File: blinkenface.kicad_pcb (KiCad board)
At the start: 2 copper layers, 135 x 50 mm, 245 parts, among them J1 CONN_01X04

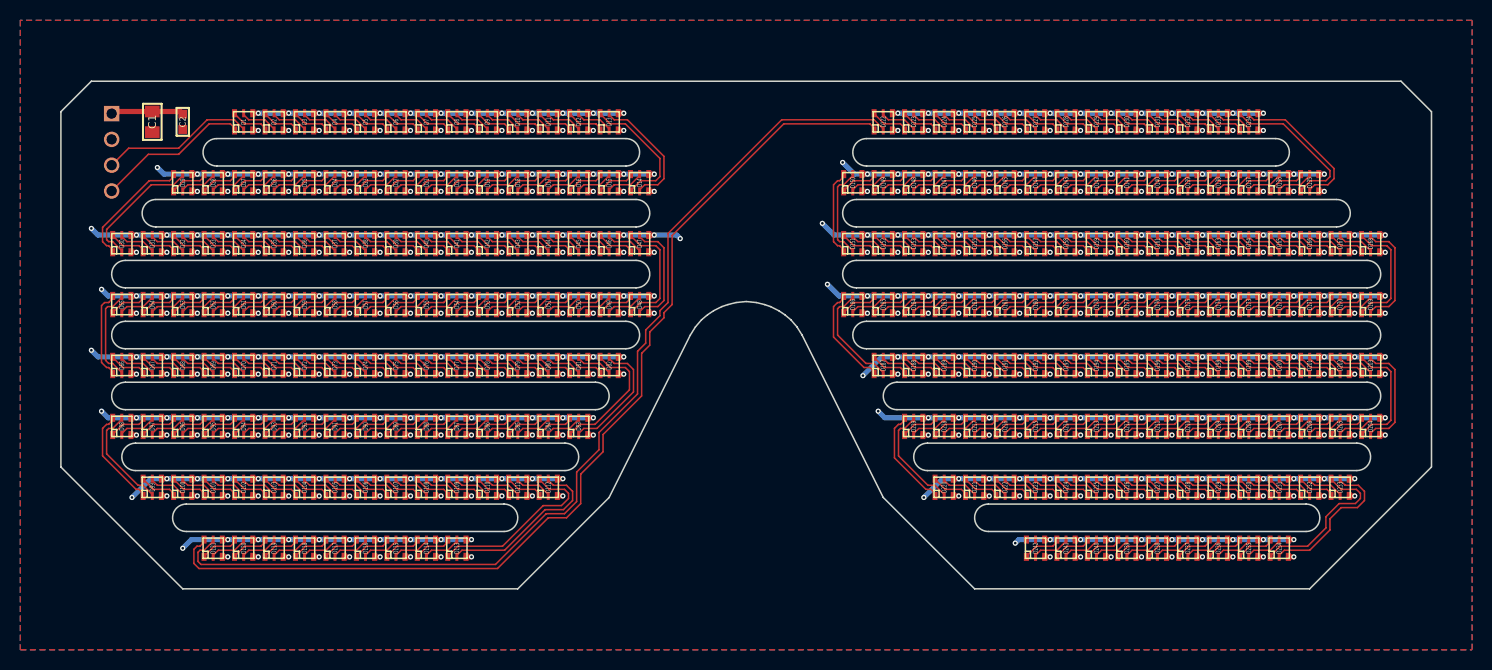
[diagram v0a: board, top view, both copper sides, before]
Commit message: fixed APA102-2020 pin order
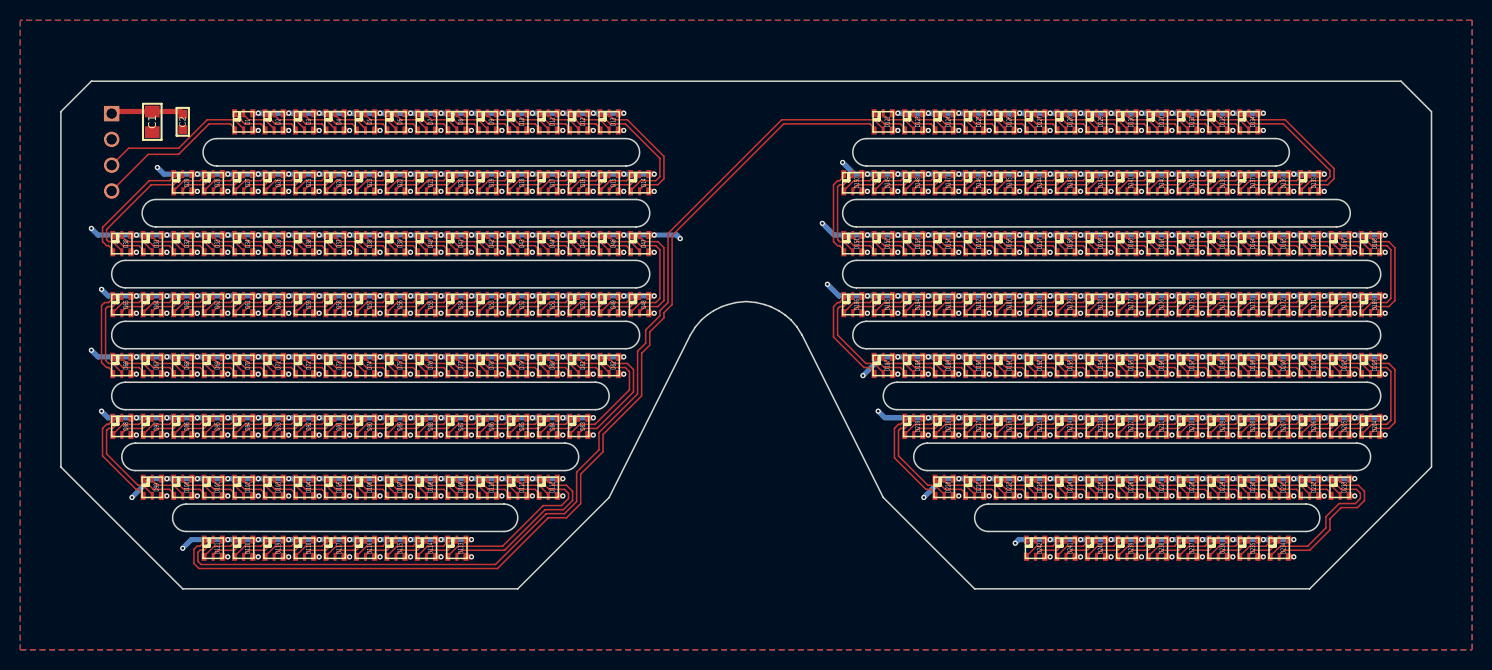
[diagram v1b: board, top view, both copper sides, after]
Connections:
- D1 pad 3: GND -> Net-(D1-Pad3)
- D1 pad 4: VCC -> GND
- D1 pad 5: Net-(D1-Pad5) -> VCC
- D10 pad 3: GND -> Net-(D10-Pad3)
- D10 pad 4: VCC -> GND
- D10 pad 5: Net-(D10-Pad5) -> VCC
- D100 pad 3: GND -> Net-(D100-Pad3)
- D100 pad 4: VCC -> GND
- D100 pad 5: Net-(D100-Pad5) -> VCC
- D101 pad 1: Net-(D100-Pad6) -> Net-(D101-Pad1)
- D101 pad 2: Net-(D100-Pad5) -> Net-(D100-Pad1)
- D101 pad 3: GND -> Net-(D100-Pad6)
- D101 pad 4: VCC -> GND
- D101 pad 5: Net-(D101-Pad5) -> VCC
- D102 pad 1: Net-(D101-Pad6) -> Net-(D102-Pad1)
- D102 pad 2: Net-(D101-Pad5) -> Net-(D101-Pad1)
- D102 pad 3: GND -> Net-(D101-Pad6)
- D102 pad 4: VCC -> GND
- D102 pad 5: Net-(D102-Pad5) -> VCC
- D103 pad 1: Net-(D102-Pad6) -> Net-(D103-Pad1)
- D103 pad 2: Net-(D102-Pad5) -> Net-(D102-Pad1)
- D103 pad 3: GND -> Net-(D102-Pad6)
- D103 pad 4: VCC -> GND
- D103 pad 5: Net-(D103-Pad5) -> VCC
- D104 pad 1: Net-(D103-Pad6) -> Net-(D104-Pad1)
- D104 pad 2: Net-(D103-Pad5) -> Net-(D103-Pad1)
- D104 pad 3: GND -> Net-(D103-Pad6)
- D104 pad 4: VCC -> GND
- D104 pad 5: Net-(D104-Pad5) -> VCC
- D105 pad 1: Net-(D104-Pad6) -> Net-(D105-Pad1)
- D105 pad 2: Net-(D104-Pad5) -> Net-(D104-Pad1)
- D105 pad 3: GND -> Net-(D104-Pad6)
- D105 pad 4: VCC -> GND
- D105 pad 5: Net-(D105-Pad5) -> VCC
- D106 pad 1: Net-(D105-Pad6) -> Net-(D106-Pad1)
- D106 pad 2: Net-(D105-Pad5) -> Net-(D105-Pad1)
- D106 pad 3: GND -> Net-(D105-Pad6)
- D106 pad 4: VCC -> GND
- D106 pad 5: Net-(D106-Pad5) -> VCC
- D107 pad 1: Net-(D106-Pad6) -> Net-(D107-Pad1)
- D107 pad 2: Net-(D106-Pad5) -> Net-(D106-Pad1)
- D107 pad 3: GND -> Net-(D106-Pad6)
- D107 pad 4: VCC -> GND
- D107 pad 5: Net-(D107-Pad5) -> VCC
- D108 pad 1: Net-(D107-Pad6) -> Net-(D108-Pad1)
- D108 pad 2: Net-(D107-Pad5) -> Net-(D107-Pad1)
- D108 pad 3: GND -> Net-(D107-Pad6)
- D108 pad 4: VCC -> GND
- D108 pad 5: Net-(D108-Pad5) -> VCC
- D109 pad 1: Net-(D108-Pad6) -> Net-(D109-Pad1)
- D109 pad 2: Net-(D108-Pad5) -> Net-(D108-Pad1)
- D109 pad 3: GND -> Net-(D108-Pad6)
- D109 pad 4: VCC -> GND
- D109 pad 5: Net-(D109-Pad5) -> VCC
- D11 pad 1: Net-(D10-Pad6) -> Net-(D11-Pad1)
- D11 pad 2: Net-(D10-Pad5) -> Net-(D10-Pad1)
- D11 pad 3: GND -> Net-(D10-Pad6)
- D11 pad 4: VCC -> GND
- D11 pad 5: Net-(D11-Pad5) -> VCC
- D110 pad 1: Net-(D109-Pad6) -> Net-(D110-Pad1)
- D110 pad 2: Net-(D109-Pad5) -> Net-(D109-Pad1)
- D110 pad 3: GND -> Net-(D109-Pad6)
- D110 pad 4: VCC -> GND
- D110 pad 5: Net-(D110-Pad5) -> VCC
- D111 pad 1: Net-(D110-Pad6) -> Net-(D111-Pad1)
- D111 pad 2: Net-(D110-Pad5) -> Net-(D110-Pad1)
- D111 pad 3: GND -> Net-(D110-Pad6)
- D111 pad 4: VCC -> GND
- D111 pad 5: Net-(D111-Pad5) -> VCC
- D112 pad 1: Net-(D111-Pad6) -> Net-(D112-Pad1)
- D112 pad 2: Net-(D111-Pad5) -> Net-(D111-Pad1)
- D112 pad 3: GND -> Net-(D111-Pad6)
- D112 pad 4: VCC -> GND
- D112 pad 5: Net-(D112-Pad5) -> VCC
- D113 pad 1: Net-(D112-Pad6) -> Net-(D113-Pad1)
- D113 pad 2: Net-(D112-Pad5) -> Net-(D112-Pad1)
- D113 pad 3: GND -> Net-(D112-Pad6)
- D113 pad 4: VCC -> GND
- D113 pad 5: Net-(D113-Pad5) -> VCC
- D114 pad 1: Net-(D113-Pad6) -> Net-(D114-Pad1)
- D114 pad 2: Net-(D113-Pad5) -> Net-(D113-Pad1)
- D114 pad 3: GND -> Net-(D113-Pad6)
- D114 pad 4: VCC -> GND
- D114 pad 5: Net-(D114-Pad5) -> VCC
- D115 pad 1: Net-(D114-Pad6) -> Net-(D115-Pad1)
- D115 pad 2: Net-(D114-Pad5) -> Net-(D114-Pad1)
- D115 pad 3: GND -> Net-(D114-Pad6)
- D115 pad 4: VCC -> GND
- D115 pad 5: Net-(D115-Pad5) -> VCC
- D116 pad 1: Net-(D115-Pad6) -> Net-(D116-Pad1)
- D116 pad 2: Net-(D115-Pad5) -> Net-(D115-Pad1)
- D116 pad 3: GND -> Net-(D115-Pad6)
- D116 pad 4: VCC -> GND
- D116 pad 5: Net-(D116-Pad5) -> VCC
- D117 pad 1: Net-(D116-Pad6) -> Net-(D117-Pad1)
- D117 pad 2: Net-(D116-Pad5) -> Net-(D116-Pad1)
- D117 pad 3: GND -> Net-(D116-Pad6)
- D117 pad 4: VCC -> GND
- D117 pad 5: Net-(D117-Pad5) -> VCC
- D118 pad 1: Net-(D117-Pad6) -> Net-(D118-Pad1)
- D118 pad 2: Net-(D117-Pad5) -> Net-(D117-Pad1)
- D118 pad 3: GND -> Net-(D117-Pad6)
- D118 pad 4: VCC -> GND
- D118 pad 5: Net-(D118-Pad5) -> VCC
- D119 pad 1: Net-(D118-Pad6) -> Net-(D119-Pad1)
- D119 pad 2: Net-(D118-Pad5) -> Net-(D118-Pad1)
- D119 pad 3: GND -> Net-(D118-Pad6)
- D119 pad 4: VCC -> GND
- D119 pad 5: Net-(D119-Pad5) -> VCC
- D12 pad 1: Net-(D11-Pad6) -> Net-(D12-Pad1)
- D12 pad 2: Net-(D11-Pad5) -> Net-(D11-Pad1)
- D12 pad 3: GND -> Net-(D11-Pad6)
- D12 pad 4: VCC -> GND
- D12 pad 5: Net-(D12-Pad5) -> VCC
- D120 pad 1: Net-(D119-Pad6) -> Net-(D120-Pad1)
- D120 pad 2: Net-(D119-Pad5) -> Net-(D119-Pad1)
- D120 pad 3: GND -> Net-(D119-Pad6)
- D120 pad 4: VCC -> GND
- D120 pad 5: Net-(D120-Pad5) -> VCC
- D121 pad 1: Net-(D120-Pad6) -> Net-(D121-Pad1)
- D121 pad 2: Net-(D120-Pad5) -> Net-(D120-Pad1)
- D121 pad 3: GND -> Net-(D120-Pad6)
- D121 pad 4: VCC -> GND
- D121 pad 5: Net-(D121-Pad5) -> VCC
- D122 pad 1: Net-(D121-Pad6) -> Net-(D122-Pad1)
- D122 pad 2: Net-(D121-Pad5) -> Net-(D121-Pad1)
- D122 pad 3: GND -> Net-(D121-Pad6)
- D122 pad 4: VCC -> GND
- D122 pad 5: Net-(D122-Pad5) -> VCC
- D123 pad 1: Net-(D122-Pad6) -> Net-(D123-Pad1)
- D123 pad 2: Net-(D122-Pad5) -> Net-(D122-Pad1)
- D123 pad 3: GND -> Net-(D122-Pad6)
- D123 pad 4: VCC -> GND
- D123 pad 5: Net-(D123-Pad5) -> VCC
- D124 pad 1: Net-(D123-Pad6) -> Net-(D124-Pad1)
- D124 pad 2: Net-(D123-Pad5) -> Net-(D123-Pad1)
- D124 pad 3: GND -> Net-(D123-Pad6)
- D124 pad 4: VCC -> GND
- D124 pad 5: Net-(D124-Pad5) -> VCC
- D125 pad 1: Net-(D124-Pad6) -> Net-(D125-Pad1)
- D125 pad 2: Net-(D124-Pad5) -> Net-(D124-Pad1)
- D125 pad 3: GND -> Net-(D124-Pad6)
- D125 pad 4: VCC -> GND
- D125 pad 5: Net-(D125-Pad5) -> VCC
- D126 pad 1: Net-(D125-Pad6) -> Net-(D126-Pad1)
- D126 pad 2: Net-(D125-Pad5) -> Net-(D125-Pad1)
- D126 pad 3: GND -> Net-(D125-Pad6)
- D126 pad 4: VCC -> GND
- D126 pad 5: Net-(D126-Pad5) -> VCC
- D127 pad 1: Net-(D126-Pad6) -> Net-(D127-Pad1)
- D127 pad 2: Net-(D126-Pad5) -> Net-(D126-Pad1)
- D127 pad 3: GND -> Net-(D126-Pad6)
- D127 pad 4: VCC -> GND
- D127 pad 5: Net-(D127-Pad5) -> VCC
- D128 pad 1: Net-(D127-Pad6) -> Net-(D128-Pad1)
- D128 pad 2: Net-(D127-Pad5) -> Net-(D127-Pad1)
- D128 pad 3: GND -> Net-(D127-Pad6)
- D128 pad 4: VCC -> GND
- D128 pad 5: Net-(D128-Pad5) -> VCC
- D129 pad 1: Net-(D128-Pad6) -> Net-(D129-Pad1)
- D129 pad 2: Net-(D128-Pad5) -> Net-(D128-Pad1)
- D129 pad 3: GND -> Net-(D128-Pad6)
- D129 pad 4: VCC -> GND
- D129 pad 5: Net-(D129-Pad5) -> VCC
- D13 pad 1: Net-(D12-Pad6) -> Net-(D13-Pad1)
- D13 pad 2: Net-(D12-Pad5) -> Net-(D12-Pad1)
- D13 pad 3: GND -> Net-(D12-Pad6)
- D13 pad 4: VCC -> GND
- D13 pad 5: Net-(D13-Pad5) -> VCC
- D130 pad 1: Net-(D129-Pad6) -> Net-(D130-Pad1)
- D130 pad 2: Net-(D129-Pad5) -> Net-(D129-Pad1)
- D130 pad 3: GND -> Net-(D129-Pad6)
- D130 pad 4: VCC -> GND
- D130 pad 5: Net-(D130-Pad5) -> VCC
- D131 pad 1: Net-(D130-Pad6) -> Net-(D131-Pad1)
- D131 pad 2: Net-(D130-Pad5) -> Net-(D130-Pad1)
- D131 pad 3: GND -> Net-(D130-Pad6)
- D131 pad 4: VCC -> GND
- D131 pad 5: Net-(D131-Pad5) -> VCC
- D132 pad 1: Net-(D131-Pad6) -> Net-(D132-Pad1)
- D132 pad 2: Net-(D131-Pad5) -> Net-(D131-Pad1)
- D132 pad 3: GND -> Net-(D131-Pad6)
- D132 pad 4: VCC -> GND
- D132 pad 5: Net-(D132-Pad5) -> VCC
- D133 pad 1: Net-(D132-Pad6) -> Net-(D133-Pad1)
- D133 pad 2: Net-(D132-Pad5) -> Net-(D132-Pad1)
- D133 pad 3: GND -> Net-(D132-Pad6)
- D133 pad 4: VCC -> GND
- D133 pad 5: Net-(D133-Pad5) -> VCC
- D134 pad 1: Net-(D133-Pad6) -> Net-(D134-Pad1)
- D134 pad 2: Net-(D133-Pad5) -> Net-(D133-Pad1)
- D134 pad 3: GND -> Net-(D133-Pad6)
- D134 pad 4: VCC -> GND
- D134 pad 5: Net-(D134-Pad5) -> VCC
- D135 pad 1: Net-(D134-Pad6) -> Net-(D135-Pad1)
- D135 pad 2: Net-(D134-Pad5) -> Net-(D134-Pad1)
- D135 pad 3: GND -> Net-(D134-Pad6)
- D135 pad 4: VCC -> GND
- D135 pad 5: Net-(D135-Pad5) -> VCC
- D136 pad 1: Net-(D135-Pad6) -> Net-(D136-Pad1)
- D136 pad 2: Net-(D135-Pad5) -> Net-(D135-Pad1)
- D136 pad 3: GND -> Net-(D135-Pad6)
- D136 pad 4: VCC -> GND
- D136 pad 5: Net-(D136-Pad5) -> VCC
- D137 pad 1: Net-(D136-Pad6) -> Net-(D137-Pad1)
- D137 pad 2: Net-(D136-Pad5) -> Net-(D136-Pad1)
- D137 pad 3: GND -> Net-(D136-Pad6)
- D137 pad 4: VCC -> GND
- D137 pad 5: Net-(D137-Pad5) -> VCC
- D138 pad 1: Net-(D137-Pad6) -> Net-(D138-Pad1)
- D138 pad 2: Net-(D137-Pad5) -> Net-(D137-Pad1)
- D138 pad 3: GND -> Net-(D137-Pad6)
- D138 pad 4: VCC -> GND
- D138 pad 5: Net-(D138-Pad5) -> VCC
- D139 pad 1: Net-(D138-Pad6) -> Net-(D139-Pad1)
- D139 pad 2: Net-(D138-Pad5) -> Net-(D138-Pad1)
- D139 pad 3: GND -> Net-(D138-Pad6)
- D139 pad 4: VCC -> GND
- D139 pad 5: Net-(D139-Pad5) -> VCC
- D14 pad 1: Net-(D13-Pad6) -> Net-(D14-Pad1)
- D14 pad 2: Net-(D13-Pad5) -> Net-(D13-Pad1)
- D14 pad 3: GND -> Net-(D13-Pad6)
- D14 pad 4: VCC -> GND
- D14 pad 5: Net-(D14-Pad5) -> VCC
- D140 pad 1: Net-(D139-Pad6) -> Net-(D140-Pad1)
- D140 pad 2: Net-(D139-Pad5) -> Net-(D139-Pad1)
- D140 pad 3: GND -> Net-(D139-Pad6)
- D140 pad 4: VCC -> GND
- D140 pad 5: Net-(D140-Pad5) -> VCC
- D141 pad 1: Net-(D140-Pad6) -> Net-(D141-Pad1)
- D141 pad 2: Net-(D140-Pad5) -> Net-(D140-Pad1)
- D141 pad 3: GND -> Net-(D140-Pad6)
- D141 pad 4: VCC -> GND
- D141 pad 5: Net-(D141-Pad5) -> VCC
- D142 pad 1: Net-(D141-Pad6) -> Net-(D142-Pad1)
- D142 pad 2: Net-(D141-Pad5) -> Net-(D141-Pad1)
- D142 pad 3: GND -> Net-(D141-Pad6)
- D142 pad 4: VCC -> GND
- D142 pad 5: Net-(D142-Pad5) -> VCC
- D143 pad 1: Net-(D142-Pad6) -> Net-(D143-Pad1)
- D143 pad 2: Net-(D142-Pad5) -> Net-(D142-Pad1)
- D143 pad 3: GND -> Net-(D142-Pad6)
- D143 pad 4: VCC -> GND
- D143 pad 5: Net-(D143-Pad5) -> VCC
- D144 pad 1: Net-(D143-Pad6) -> Net-(D144-Pad1)
- D144 pad 2: Net-(D143-Pad5) -> Net-(D143-Pad1)
- D144 pad 3: GND -> Net-(D143-Pad6)
- D144 pad 4: VCC -> GND
- D144 pad 5: Net-(D144-Pad5) -> VCC
- D145 pad 1: Net-(D144-Pad6) -> Net-(D145-Pad1)
- D145 pad 2: Net-(D144-Pad5) -> Net-(D144-Pad1)
- D145 pad 3: GND -> Net-(D144-Pad6)
- D145 pad 4: VCC -> GND
- D145 pad 5: Net-(D145-Pad5) -> VCC
- D146 pad 1: Net-(D145-Pad6) -> Net-(D146-Pad1)
- D146 pad 2: Net-(D145-Pad5) -> Net-(D145-Pad1)
- D146 pad 3: GND -> Net-(D145-Pad6)
- D146 pad 4: VCC -> GND
- D146 pad 5: Net-(D146-Pad5) -> VCC
- D147 pad 1: Net-(D146-Pad6) -> Net-(D147-Pad1)
- D147 pad 2: Net-(D146-Pad5) -> Net-(D146-Pad1)
- D147 pad 3: GND -> Net-(D146-Pad6)
- D147 pad 4: VCC -> GND
- D147 pad 5: Net-(D147-Pad5) -> VCC
- D148 pad 1: Net-(D147-Pad6) -> Net-(D148-Pad1)
- D148 pad 2: Net-(D147-Pad5) -> Net-(D147-Pad1)
- D148 pad 3: GND -> Net-(D147-Pad6)
- D148 pad 4: VCC -> GND
- D148 pad 5: Net-(D148-Pad5) -> VCC
- D149 pad 1: Net-(D148-Pad6) -> Net-(D149-Pad1)
- D149 pad 2: Net-(D148-Pad5) -> Net-(D148-Pad1)
- D149 pad 3: GND -> Net-(D148-Pad6)
- D149 pad 4: VCC -> GND
- D149 pad 5: Net-(D149-Pad5) -> VCC
- D15 pad 1: Net-(D14-Pad6) -> Net-(D15-Pad1)
- D15 pad 2: Net-(D14-Pad5) -> Net-(D14-Pad1)
- D15 pad 3: GND -> Net-(D14-Pad6)
- D15 pad 4: VCC -> GND
- D15 pad 5: Net-(D15-Pad5) -> VCC
- D150 pad 1: Net-(D149-Pad6) -> Net-(D150-Pad1)
- D150 pad 2: Net-(D149-Pad5) -> Net-(D149-Pad1)
- D150 pad 3: GND -> Net-(D149-Pad6)
- D150 pad 4: VCC -> GND
- D150 pad 5: Net-(D150-Pad5) -> VCC
- D151 pad 1: Net-(D150-Pad6) -> Net-(D151-Pad1)
- D151 pad 2: Net-(D150-Pad5) -> Net-(D150-Pad1)
- D151 pad 3: GND -> Net-(D150-Pad6)
- D151 pad 4: VCC -> GND
- D151 pad 5: Net-(D151-Pad5) -> VCC
- D152 pad 1: Net-(D151-Pad6) -> Net-(D152-Pad1)
- D152 pad 2: Net-(D151-Pad5) -> Net-(D151-Pad1)
- D152 pad 3: GND -> Net-(D151-Pad6)
- D152 pad 4: VCC -> GND
- D152 pad 5: Net-(D152-Pad5) -> VCC
- D153 pad 1: Net-(D152-Pad6) -> Net-(D153-Pad1)
- D153 pad 2: Net-(D152-Pad5) -> Net-(D152-Pad1)
- D153 pad 3: GND -> Net-(D152-Pad6)
- D153 pad 4: VCC -> GND
- D153 pad 5: Net-(D153-Pad5) -> VCC
- D154 pad 1: Net-(D153-Pad6) -> Net-(D154-Pad1)
- D154 pad 2: Net-(D153-Pad5) -> Net-(D153-Pad1)
- D154 pad 3: GND -> Net-(D153-Pad6)
- D154 pad 4: VCC -> GND
- D154 pad 5: Net-(D154-Pad5) -> VCC
- D155 pad 1: Net-(D154-Pad6) -> Net-(D155-Pad1)
- D155 pad 2: Net-(D154-Pad5) -> Net-(D154-Pad1)
- D155 pad 3: GND -> Net-(D154-Pad6)
- D155 pad 4: VCC -> GND
- D155 pad 5: Net-(D155-Pad5) -> VCC
- D156 pad 1: Net-(D155-Pad6) -> Net-(D156-Pad1)
- D156 pad 2: Net-(D155-Pad5) -> Net-(D155-Pad1)
- D156 pad 3: GND -> Net-(D155-Pad6)
- D156 pad 4: VCC -> GND
- D156 pad 5: Net-(D156-Pad5) -> VCC
- D157 pad 1: Net-(D156-Pad6) -> Net-(D157-Pad1)
- D157 pad 2: Net-(D156-Pad5) -> Net-(D156-Pad1)
- D157 pad 3: GND -> Net-(D156-Pad6)
- D157 pad 4: VCC -> GND
- D157 pad 5: Net-(D157-Pad5) -> VCC
- D158 pad 1: Net-(D157-Pad6) -> Net-(D158-Pad1)
- D158 pad 2: Net-(D157-Pad5) -> Net-(D157-Pad1)
- D158 pad 3: GND -> Net-(D157-Pad6)
- D158 pad 4: VCC -> GND
- D158 pad 5: Net-(D158-Pad5) -> VCC
- D159 pad 1: Net-(D158-Pad6) -> Net-(D159-Pad1)
- D159 pad 2: Net-(D158-Pad5) -> Net-(D158-Pad1)
- D159 pad 3: GND -> Net-(D158-Pad6)
- D159 pad 4: VCC -> GND
- D159 pad 5: Net-(D159-Pad5) -> VCC
- D16 pad 1: Net-(D15-Pad6) -> Net-(D16-Pad1)
- D16 pad 2: Net-(D15-Pad5) -> Net-(D15-Pad1)
- D16 pad 3: GND -> Net-(D15-Pad6)
- D16 pad 4: VCC -> GND
- D16 pad 5: Net-(D16-Pad5) -> VCC
- D160 pad 1: Net-(D159-Pad6) -> Net-(D160-Pad1)
- D160 pad 2: Net-(D159-Pad5) -> Net-(D159-Pad1)
- D160 pad 3: GND -> Net-(D159-Pad6)
- D160 pad 4: VCC -> GND
- D160 pad 5: Net-(D160-Pad5) -> VCC
- D161 pad 1: Net-(D160-Pad6) -> Net-(D161-Pad1)
- D161 pad 2: Net-(D160-Pad5) -> Net-(D160-Pad1)
- D161 pad 3: GND -> Net-(D160-Pad6)
- D161 pad 4: VCC -> GND
- D161 pad 5: Net-(D161-Pad5) -> VCC
- D162 pad 1: Net-(D161-Pad6) -> Net-(D162-Pad1)
- D162 pad 2: Net-(D161-Pad5) -> Net-(D161-Pad1)
- D162 pad 3: GND -> Net-(D161-Pad6)
- D162 pad 4: VCC -> GND
- D162 pad 5: Net-(D162-Pad5) -> VCC
- D163 pad 1: Net-(D162-Pad6) -> Net-(D163-Pad1)
- D163 pad 2: Net-(D162-Pad5) -> Net-(D162-Pad1)
- D163 pad 3: GND -> Net-(D162-Pad6)
- D163 pad 4: VCC -> GND
- D163 pad 5: Net-(D163-Pad5) -> VCC
- D164 pad 1: Net-(D163-Pad6) -> Net-(D164-Pad1)
- D164 pad 2: Net-(D163-Pad5) -> Net-(D163-Pad1)
- D164 pad 3: GND -> Net-(D163-Pad6)
- D164 pad 4: VCC -> GND
- D164 pad 5: Net-(D164-Pad5) -> VCC
- D165 pad 1: Net-(D164-Pad6) -> Net-(D165-Pad1)
- D165 pad 2: Net-(D164-Pad5) -> Net-(D164-Pad1)
- D165 pad 3: GND -> Net-(D164-Pad6)
- D165 pad 4: VCC -> GND
- D165 pad 5: Net-(D165-Pad5) -> VCC
- D166 pad 1: Net-(D165-Pad6) -> Net-(D166-Pad1)
- D166 pad 2: Net-(D165-Pad5) -> Net-(D165-Pad1)
- D166 pad 3: GND -> Net-(D165-Pad6)
- D166 pad 4: VCC -> GND
- D166 pad 5: Net-(D166-Pad5) -> VCC
- D167 pad 1: Net-(D166-Pad6) -> Net-(D167-Pad1)
- D167 pad 2: Net-(D166-Pad5) -> Net-(D166-Pad1)
- D167 pad 3: GND -> Net-(D166-Pad6)
- D167 pad 4: VCC -> GND
- D167 pad 5: Net-(D167-Pad5) -> VCC
- D168 pad 1: Net-(D167-Pad6) -> Net-(D168-Pad1)
- D168 pad 2: Net-(D167-Pad5) -> Net-(D167-Pad1)
- D168 pad 3: GND -> Net-(D167-Pad6)
- D168 pad 4: VCC -> GND
- D168 pad 5: Net-(D168-Pad5) -> VCC
- D169 pad 1: Net-(D168-Pad6) -> Net-(D169-Pad1)
- D169 pad 2: Net-(D168-Pad5) -> Net-(D168-Pad1)
- D169 pad 3: GND -> Net-(D168-Pad6)
- D169 pad 4: VCC -> GND
- D169 pad 5: Net-(D169-Pad5) -> VCC
- D17 pad 1: Net-(D16-Pad6) -> Net-(D17-Pad1)
- D17 pad 2: Net-(D16-Pad5) -> Net-(D16-Pad1)
- D17 pad 3: GND -> Net-(D16-Pad6)
- D17 pad 4: VCC -> GND
- D17 pad 5: Net-(D17-Pad5) -> VCC
- D170 pad 1: Net-(D169-Pad6) -> Net-(D170-Pad1)
- D170 pad 2: Net-(D169-Pad5) -> Net-(D169-Pad1)
- D170 pad 3: GND -> Net-(D169-Pad6)
- D170 pad 4: VCC -> GND
- D170 pad 5: Net-(D170-Pad5) -> VCC
- D171 pad 1: Net-(D170-Pad6) -> Net-(D171-Pad1)
- D171 pad 2: Net-(D170-Pad5) -> Net-(D170-Pad1)
- D171 pad 3: GND -> Net-(D170-Pad6)
- D171 pad 4: VCC -> GND
- D171 pad 5: Net-(D171-Pad5) -> VCC
- D172 pad 1: Net-(D171-Pad6) -> Net-(D172-Pad1)
- D172 pad 2: Net-(D171-Pad5) -> Net-(D171-Pad1)
- D172 pad 3: GND -> Net-(D171-Pad6)
- D172 pad 4: VCC -> GND
- D172 pad 5: Net-(D172-Pad5) -> VCC
- D173 pad 1: Net-(D172-Pad6) -> Net-(D173-Pad1)
- D173 pad 2: Net-(D172-Pad5) -> Net-(D172-Pad1)
- D173 pad 3: GND -> Net-(D172-Pad6)
- D173 pad 4: VCC -> GND
- D173 pad 5: Net-(D173-Pad5) -> VCC
- D174 pad 1: Net-(D173-Pad6) -> Net-(D174-Pad1)
- D174 pad 2: Net-(D173-Pad5) -> Net-(D173-Pad1)
- D174 pad 3: GND -> Net-(D173-Pad6)
- D174 pad 4: VCC -> GND
- D174 pad 5: Net-(D174-Pad5) -> VCC
- D175 pad 1: Net-(D174-Pad6) -> Net-(D175-Pad1)
- D175 pad 2: Net-(D174-Pad5) -> Net-(D174-Pad1)
- D175 pad 3: GND -> Net-(D174-Pad6)
- D175 pad 4: VCC -> GND
- D175 pad 5: Net-(D175-Pad5) -> VCC
- D176 pad 1: Net-(D175-Pad6) -> Net-(D176-Pad1)
- D176 pad 2: Net-(D175-Pad5) -> Net-(D175-Pad1)
- D176 pad 3: GND -> Net-(D175-Pad6)
- D176 pad 4: VCC -> GND
- D176 pad 5: Net-(D176-Pad5) -> VCC
- D177 pad 1: Net-(D176-Pad6) -> Net-(D177-Pad1)
- D177 pad 2: Net-(D176-Pad5) -> Net-(D176-Pad1)
- D177 pad 3: GND -> Net-(D176-Pad6)
- D177 pad 4: VCC -> GND
- D177 pad 5: Net-(D177-Pad5) -> VCC
- D178 pad 1: Net-(D177-Pad6) -> Net-(D178-Pad1)
- D178 pad 2: Net-(D177-Pad5) -> Net-(D177-Pad1)
- D178 pad 3: GND -> Net-(D177-Pad6)
- D178 pad 4: VCC -> GND
- D178 pad 5: Net-(D178-Pad5) -> VCC
- D179 pad 1: Net-(D178-Pad6) -> Net-(D179-Pad1)
- D179 pad 2: Net-(D178-Pad5) -> Net-(D178-Pad1)
- D179 pad 3: GND -> Net-(D178-Pad6)
- D179 pad 4: VCC -> GND
- D179 pad 5: Net-(D179-Pad5) -> VCC
- D18 pad 1: Net-(D17-Pad6) -> Net-(D18-Pad1)
- D18 pad 2: Net-(D17-Pad5) -> Net-(D17-Pad1)
- D18 pad 3: GND -> Net-(D17-Pad6)
- D18 pad 4: VCC -> GND
- D18 pad 5: Net-(D18-Pad5) -> VCC
- D180 pad 1: Net-(D179-Pad6) -> Net-(D180-Pad1)
- D180 pad 2: Net-(D179-Pad5) -> Net-(D179-Pad1)
- D180 pad 3: GND -> Net-(D179-Pad6)
- D180 pad 4: VCC -> GND
- D180 pad 5: Net-(D180-Pad5) -> VCC
- D181 pad 1: Net-(D180-Pad6) -> Net-(D181-Pad1)
- D181 pad 2: Net-(D180-Pad5) -> Net-(D180-Pad1)
- D181 pad 3: GND -> Net-(D180-Pad6)
- D181 pad 4: VCC -> GND
- D181 pad 5: Net-(D181-Pad5) -> VCC
- D182 pad 1: Net-(D181-Pad6) -> Net-(D182-Pad1)
- D182 pad 2: Net-(D181-Pad5) -> Net-(D181-Pad1)
- D182 pad 3: GND -> Net-(D181-Pad6)
- D182 pad 4: VCC -> GND
- D182 pad 5: Net-(D182-Pad5) -> VCC
- D183 pad 1: Net-(D182-Pad6) -> Net-(D183-Pad1)
- D183 pad 2: Net-(D182-Pad5) -> Net-(D182-Pad1)
- D183 pad 3: GND -> Net-(D182-Pad6)
- D183 pad 4: VCC -> GND
- D183 pad 5: Net-(D183-Pad5) -> VCC
- D184 pad 1: Net-(D183-Pad6) -> Net-(D184-Pad1)
- D184 pad 2: Net-(D183-Pad5) -> Net-(D183-Pad1)
- D184 pad 3: GND -> Net-(D183-Pad6)
- D184 pad 4: VCC -> GND
- D184 pad 5: Net-(D184-Pad5) -> VCC
- D185 pad 1: Net-(D184-Pad6) -> Net-(D185-Pad1)
- D185 pad 2: Net-(D184-Pad5) -> Net-(D184-Pad1)
- D185 pad 3: GND -> Net-(D184-Pad6)
- D185 pad 4: VCC -> GND
- D185 pad 5: Net-(D185-Pad5) -> VCC
- D186 pad 1: Net-(D185-Pad6) -> Net-(D186-Pad1)
- D186 pad 2: Net-(D185-Pad5) -> Net-(D185-Pad1)
- D186 pad 3: GND -> Net-(D185-Pad6)
- D186 pad 4: VCC -> GND
- D186 pad 5: Net-(D186-Pad5) -> VCC
- D187 pad 1: Net-(D186-Pad6) -> Net-(D187-Pad1)
- D187 pad 2: Net-(D186-Pad5) -> Net-(D186-Pad1)
- D187 pad 3: GND -> Net-(D186-Pad6)
- D187 pad 4: VCC -> GND
- D187 pad 5: Net-(D187-Pad5) -> VCC
- D188 pad 1: Net-(D187-Pad6) -> Net-(D188-Pad1)
- D188 pad 2: Net-(D187-Pad5) -> Net-(D187-Pad1)
- D188 pad 3: GND -> Net-(D187-Pad6)
- D188 pad 4: VCC -> GND
- D188 pad 5: Net-(D188-Pad5) -> VCC
- D189 pad 1: Net-(D188-Pad6) -> Net-(D189-Pad1)
- D189 pad 2: Net-(D188-Pad5) -> Net-(D188-Pad1)
- D189 pad 3: GND -> Net-(D188-Pad6)
- D189 pad 4: VCC -> GND
- D189 pad 5: Net-(D189-Pad5) -> VCC
- D19 pad 1: Net-(D18-Pad6) -> Net-(D19-Pad1)
- D19 pad 2: Net-(D18-Pad5) -> Net-(D18-Pad1)
- D19 pad 3: GND -> Net-(D18-Pad6)
- D19 pad 4: VCC -> GND
- D19 pad 5: Net-(D19-Pad5) -> VCC
- D190 pad 1: Net-(D189-Pad6) -> Net-(D190-Pad1)
- D190 pad 2: Net-(D189-Pad5) -> Net-(D189-Pad1)
- D190 pad 3: GND -> Net-(D189-Pad6)
- D190 pad 4: VCC -> GND
- D190 pad 5: Net-(D190-Pad5) -> VCC
- D191 pad 1: Net-(D190-Pad6) -> Net-(D191-Pad1)
- D191 pad 2: Net-(D190-Pad5) -> Net-(D190-Pad1)
- D191 pad 3: GND -> Net-(D190-Pad6)
- D191 pad 4: VCC -> GND
- D191 pad 5: Net-(D191-Pad5) -> VCC
- D192 pad 1: Net-(D191-Pad6) -> Net-(D192-Pad1)
- D192 pad 2: Net-(D191-Pad5) -> Net-(D191-Pad1)
- D192 pad 3: GND -> Net-(D191-Pad6)
- D192 pad 4: VCC -> GND
- D192 pad 5: Net-(D192-Pad5) -> VCC
- D193 pad 1: Net-(D192-Pad6) -> Net-(D193-Pad1)
- D193 pad 2: Net-(D192-Pad5) -> Net-(D192-Pad1)
- D193 pad 3: GND -> Net-(D192-Pad6)
- D193 pad 4: VCC -> GND
- D193 pad 5: Net-(D193-Pad5) -> VCC
- D194 pad 1: Net-(D193-Pad6) -> Net-(D194-Pad1)
- D194 pad 2: Net-(D193-Pad5) -> Net-(D193-Pad1)
- D194 pad 3: GND -> Net-(D193-Pad6)
- D194 pad 4: VCC -> GND
- D194 pad 5: Net-(D194-Pad5) -> VCC
- D195 pad 1: Net-(D194-Pad6) -> Net-(D195-Pad1)
- D195 pad 2: Net-(D194-Pad5) -> Net-(D194-Pad1)
- D195 pad 3: GND -> Net-(D194-Pad6)
- D195 pad 4: VCC -> GND
- D195 pad 5: Net-(D195-Pad5) -> VCC
- D196 pad 1: Net-(D195-Pad6) -> Net-(D196-Pad1)
- D196 pad 2: Net-(D195-Pad5) -> Net-(D195-Pad1)
- D196 pad 3: GND -> Net-(D195-Pad6)
- D196 pad 4: VCC -> GND
- D196 pad 5: Net-(D196-Pad5) -> VCC
- D197 pad 1: Net-(D196-Pad6) -> Net-(D197-Pad1)
- D197 pad 2: Net-(D196-Pad5) -> Net-(D196-Pad1)
- D197 pad 3: GND -> Net-(D196-Pad6)
- D197 pad 4: VCC -> GND
- D197 pad 5: Net-(D197-Pad5) -> VCC
- D198 pad 1: Net-(D197-Pad6) -> Net-(D198-Pad1)
- D198 pad 2: Net-(D197-Pad5) -> Net-(D197-Pad1)
- D198 pad 3: GND -> Net-(D197-Pad6)
- D198 pad 4: VCC -> GND
- D198 pad 5: Net-(D198-Pad5) -> VCC
- D199 pad 1: Net-(D198-Pad6) -> Net-(D199-Pad1)
- D199 pad 2: Net-(D198-Pad5) -> Net-(D198-Pad1)
- D199 pad 3: GND -> Net-(D198-Pad6)
- D199 pad 4: VCC -> GND
- D199 pad 5: Net-(D199-Pad5) -> VCC
- D2 pad 1: Net-(D1-Pad6) -> Net-(D2-Pad1)
- D2 pad 2: Net-(D1-Pad5) -> Net-(D1-Pad1)
- D2 pad 3: GND -> Net-(D1-Pad6)
- D2 pad 4: VCC -> GND
- D2 pad 5: Net-(D2-Pad5) -> VCC
- D20 pad 1: Net-(D19-Pad6) -> Net-(D20-Pad1)
- D20 pad 2: Net-(D19-Pad5) -> Net-(D19-Pad1)
- D20 pad 3: GND -> Net-(D19-Pad6)
- D20 pad 4: VCC -> GND
- D20 pad 5: Net-(D20-Pad5) -> VCC
- D200 pad 1: Net-(D199-Pad6) -> Net-(D200-Pad1)
- D200 pad 2: Net-(D199-Pad5) -> Net-(D199-Pad1)
- D200 pad 3: GND -> Net-(D199-Pad6)
- D200 pad 4: VCC -> GND
- D200 pad 5: Net-(D200-Pad5) -> VCC
- D201 pad 1: Net-(D200-Pad6) -> Net-(D201-Pad1)
- D201 pad 2: Net-(D200-Pad5) -> Net-(D200-Pad1)
- D201 pad 3: GND -> Net-(D200-Pad6)
- D201 pad 4: VCC -> GND
- D201 pad 5: Net-(D201-Pad5) -> VCC
- D202 pad 1: Net-(D201-Pad6) -> Net-(D202-Pad1)
- D202 pad 2: Net-(D201-Pad5) -> Net-(D201-Pad1)
- D202 pad 3: GND -> Net-(D201-Pad6)
- D202 pad 4: VCC -> GND
- D202 pad 5: Net-(D202-Pad5) -> VCC
- D203 pad 1: Net-(D202-Pad6) -> Net-(D203-Pad1)
- D203 pad 2: Net-(D202-Pad5) -> Net-(D202-Pad1)
- D203 pad 3: GND -> Net-(D202-Pad6)
- D203 pad 4: VCC -> GND
- D203 pad 5: Net-(D203-Pad5) -> VCC
- D204 pad 1: Net-(D203-Pad6) -> Net-(D204-Pad1)
- D204 pad 2: Net-(D203-Pad5) -> Net-(D203-Pad1)
- D204 pad 3: GND -> Net-(D203-Pad6)
- D204 pad 4: VCC -> GND
- D204 pad 5: Net-(D204-Pad5) -> VCC
- D205 pad 1: Net-(D204-Pad6) -> Net-(D205-Pad1)
- D205 pad 2: Net-(D204-Pad5) -> Net-(D204-Pad1)
- D205 pad 3: GND -> Net-(D204-Pad6)
- D205 pad 4: VCC -> GND
- D205 pad 5: Net-(D205-Pad5) -> VCC
- D206 pad 1: Net-(D205-Pad6) -> Net-(D206-Pad1)
- D206 pad 2: Net-(D205-Pad5) -> Net-(D205-Pad1)
- D206 pad 3: GND -> Net-(D205-Pad6)
- D206 pad 4: VCC -> GND
- D206 pad 5: Net-(D206-Pad5) -> VCC
- D207 pad 1: Net-(D206-Pad6) -> Net-(D207-Pad1)
- D207 pad 2: Net-(D206-Pad5) -> Net-(D206-Pad1)
- D207 pad 3: GND -> Net-(D206-Pad6)
- D207 pad 4: VCC -> GND
- D207 pad 5: Net-(D207-Pad5) -> VCC
- D208 pad 1: Net-(D207-Pad6) -> Net-(D208-Pad1)
- D208 pad 2: Net-(D207-Pad5) -> Net-(D207-Pad1)
- D208 pad 3: GND -> Net-(D207-Pad6)
- D208 pad 4: VCC -> GND
- D208 pad 5: Net-(D208-Pad5) -> VCC
- D209 pad 1: Net-(D208-Pad6) -> Net-(D209-Pad1)
- D209 pad 2: Net-(D208-Pad5) -> Net-(D208-Pad1)
- D209 pad 3: GND -> Net-(D208-Pad6)
- D209 pad 4: VCC -> GND
- D209 pad 5: Net-(D209-Pad5) -> VCC
- D21 pad 1: Net-(D20-Pad6) -> Net-(D21-Pad1)
- D21 pad 2: Net-(D20-Pad5) -> Net-(D20-Pad1)
- D21 pad 3: GND -> Net-(D20-Pad6)
- D21 pad 4: VCC -> GND
- D21 pad 5: Net-(D21-Pad5) -> VCC
- D210 pad 1: Net-(D209-Pad6) -> Net-(D210-Pad1)
- D210 pad 2: Net-(D209-Pad5) -> Net-(D209-Pad1)
- D210 pad 3: GND -> Net-(D209-Pad6)
- D210 pad 4: VCC -> GND
- D210 pad 5: Net-(D210-Pad5) -> VCC
- D211 pad 1: Net-(D210-Pad6) -> Net-(D211-Pad1)
- D211 pad 2: Net-(D210-Pad5) -> Net-(D210-Pad1)
- D211 pad 3: GND -> Net-(D210-Pad6)
- D211 pad 4: VCC -> GND
- D211 pad 5: Net-(D211-Pad5) -> VCC
- D212 pad 1: Net-(D211-Pad6) -> Net-(D212-Pad1)
- D212 pad 2: Net-(D211-Pad5) -> Net-(D211-Pad1)
- D212 pad 3: GND -> Net-(D211-Pad6)
- D212 pad 4: VCC -> GND
- D212 pad 5: Net-(D212-Pad5) -> VCC
- D213 pad 1: Net-(D212-Pad6) -> Net-(D213-Pad1)
- D213 pad 2: Net-(D212-Pad5) -> Net-(D212-Pad1)
- D213 pad 3: GND -> Net-(D212-Pad6)
- D213 pad 4: VCC -> GND
- D213 pad 5: Net-(D213-Pad5) -> VCC
- D214 pad 1: Net-(D213-Pad6) -> Net-(D214-Pad1)
- D214 pad 2: Net-(D213-Pad5) -> Net-(D213-Pad1)
- D214 pad 3: GND -> Net-(D213-Pad6)
- D214 pad 4: VCC -> GND
- D214 pad 5: Net-(D214-Pad5) -> VCC
- D215 pad 1: Net-(D214-Pad6) -> Net-(D215-Pad1)
- D215 pad 2: Net-(D214-Pad5) -> Net-(D214-Pad1)
- D215 pad 3: GND -> Net-(D214-Pad6)
- D215 pad 4: VCC -> GND
- D215 pad 5: Net-(D215-Pad5) -> VCC
- D216 pad 1: Net-(D215-Pad6) -> Net-(D216-Pad1)
- D216 pad 2: Net-(D215-Pad5) -> Net-(D215-Pad1)
- D216 pad 3: GND -> Net-(D215-Pad6)
- D216 pad 4: VCC -> GND
- D216 pad 5: Net-(D216-Pad5) -> VCC
- D217 pad 1: Net-(D216-Pad6) -> Net-(D217-Pad1)
- D217 pad 2: Net-(D216-Pad5) -> Net-(D216-Pad1)
- D217 pad 3: GND -> Net-(D216-Pad6)
- D217 pad 4: VCC -> GND
- D217 pad 5: Net-(D217-Pad5) -> VCC
- D218 pad 1: Net-(D217-Pad6) -> Net-(D218-Pad1)
- D218 pad 2: Net-(D217-Pad5) -> Net-(D217-Pad1)
- D218 pad 3: GND -> Net-(D217-Pad6)
- D218 pad 4: VCC -> GND
- D218 pad 5: Net-(D218-Pad5) -> VCC
- D219 pad 1: Net-(D218-Pad6) -> Net-(D219-Pad1)
- D219 pad 2: Net-(D218-Pad5) -> Net-(D218-Pad1)
- D219 pad 3: GND -> Net-(D218-Pad6)
- D219 pad 4: VCC -> GND
- D219 pad 5: Net-(D219-Pad5) -> VCC
- D22 pad 1: Net-(D21-Pad6) -> Net-(D22-Pad1)
- D22 pad 2: Net-(D21-Pad5) -> Net-(D21-Pad1)
- D22 pad 3: GND -> Net-(D21-Pad6)
- D22 pad 4: VCC -> GND
- D22 pad 5: Net-(D22-Pad5) -> VCC
- D220 pad 1: Net-(D219-Pad6) -> Net-(D220-Pad1)
- D220 pad 2: Net-(D219-Pad5) -> Net-(D219-Pad1)
- D220 pad 3: GND -> Net-(D219-Pad6)
- D220 pad 4: VCC -> GND
- D220 pad 5: Net-(D220-Pad5) -> VCC
- D221 pad 1: Net-(D220-Pad6) -> Net-(D221-Pad1)
- D221 pad 2: Net-(D220-Pad5) -> Net-(D220-Pad1)
- D221 pad 3: GND -> Net-(D220-Pad6)
- D221 pad 4: VCC -> GND
- D221 pad 5: Net-(D221-Pad5) -> VCC
- D222 pad 1: Net-(D221-Pad6) -> Net-(D222-Pad1)
- D222 pad 2: Net-(D221-Pad5) -> Net-(D221-Pad1)
- D222 pad 3: GND -> Net-(D221-Pad6)
- D222 pad 4: VCC -> GND
- D222 pad 5: Net-(D222-Pad5) -> VCC
- D223 pad 1: Net-(D222-Pad6) -> Net-(D223-Pad1)
- D223 pad 2: Net-(D222-Pad5) -> Net-(D222-Pad1)
- D223 pad 3: GND -> Net-(D222-Pad6)
- D223 pad 4: VCC -> GND
- D223 pad 5: Net-(D223-Pad5) -> VCC
- D224 pad 1: Net-(D223-Pad6) -> Net-(D224-Pad1)
- D224 pad 2: Net-(D223-Pad5) -> Net-(D223-Pad1)
- D224 pad 3: GND -> Net-(D223-Pad6)
- D224 pad 4: VCC -> GND
- D224 pad 5: Net-(D224-Pad5) -> VCC
- D225 pad 1: Net-(D224-Pad6) -> Net-(D225-Pad1)
- D225 pad 2: Net-(D224-Pad5) -> Net-(D224-Pad1)
- D225 pad 3: GND -> Net-(D224-Pad6)
- D225 pad 4: VCC -> GND
- D225 pad 5: Net-(D225-Pad5) -> VCC
- D226 pad 1: Net-(D225-Pad6) -> Net-(D226-Pad1)
- D226 pad 2: Net-(D225-Pad5) -> Net-(D225-Pad1)
- D226 pad 3: GND -> Net-(D225-Pad6)
- D226 pad 4: VCC -> GND
- D226 pad 5: Net-(D226-Pad5) -> VCC
- D227 pad 1: Net-(D226-Pad6) -> Net-(D227-Pad1)
- D227 pad 2: Net-(D226-Pad5) -> Net-(D226-Pad1)
- D227 pad 3: GND -> Net-(D226-Pad6)
- D227 pad 4: VCC -> GND
- D227 pad 5: Net-(D227-Pad5) -> VCC
- D228 pad 1: Net-(D227-Pad6) -> Net-(D228-Pad1)
- D228 pad 2: Net-(D227-Pad5) -> Net-(D227-Pad1)
- D228 pad 3: GND -> Net-(D227-Pad6)
- D228 pad 4: VCC -> GND
- D228 pad 5: Net-(D228-Pad5) -> VCC
- D229 pad 1: Net-(D228-Pad6) -> Net-(D229-Pad1)
- D229 pad 2: Net-(D228-Pad5) -> Net-(D228-Pad1)
- D229 pad 3: GND -> Net-(D228-Pad6)
- D229 pad 4: VCC -> GND
- D229 pad 5: Net-(D229-Pad5) -> VCC
- D23 pad 1: Net-(D22-Pad6) -> Net-(D23-Pad1)
- D23 pad 2: Net-(D22-Pad5) -> Net-(D22-Pad1)
- D23 pad 3: GND -> Net-(D22-Pad6)
- D23 pad 4: VCC -> GND
- D23 pad 5: Net-(D23-Pad5) -> VCC
- D230 pad 1: Net-(D229-Pad6) -> Net-(D230-Pad1)
- D230 pad 2: Net-(D229-Pad5) -> Net-(D229-Pad1)
- D230 pad 3: GND -> Net-(D229-Pad6)
- D230 pad 4: VCC -> GND
- D230 pad 5: Net-(D230-Pad5) -> VCC
- D231 pad 1: Net-(D230-Pad6) -> Net-(D231-Pad1)
- D231 pad 2: Net-(D230-Pad5) -> Net-(D230-Pad1)
- D231 pad 3: GND -> Net-(D230-Pad6)
- D231 pad 4: VCC -> GND
- D231 pad 5: Net-(D231-Pad5) -> VCC
- D232 pad 1: Net-(D231-Pad6) -> Net-(D232-Pad1)
- D232 pad 2: Net-(D231-Pad5) -> Net-(D231-Pad1)
- D232 pad 3: GND -> Net-(D231-Pad6)
- D232 pad 4: VCC -> GND
- D232 pad 5: Net-(D232-Pad5) -> VCC
- D233 pad 1: Net-(D232-Pad6) -> Net-(D233-Pad1)
- D233 pad 2: Net-(D232-Pad5) -> Net-(D232-Pad1)
- D233 pad 3: GND -> Net-(D232-Pad6)
- D233 pad 4: VCC -> GND
- D233 pad 5: Net-(D233-Pad5) -> VCC
- D234 pad 1: Net-(D233-Pad6) -> Net-(D234-Pad1)
- D234 pad 2: Net-(D233-Pad5) -> Net-(D233-Pad1)
- D234 pad 3: GND -> Net-(D233-Pad6)
- D234 pad 4: VCC -> GND
- D234 pad 5: Net-(D234-Pad5) -> VCC
- D235 pad 1: Net-(D234-Pad6) -> Net-(D235-Pad1)
- D235 pad 2: Net-(D234-Pad5) -> Net-(D234-Pad1)
- D235 pad 3: GND -> Net-(D234-Pad6)
- D235 pad 4: VCC -> GND
- D235 pad 5: Net-(D235-Pad5) -> VCC
- D236 pad 1: Net-(D235-Pad6) -> Net-(D236-Pad1)
- D236 pad 2: Net-(D235-Pad5) -> Net-(D235-Pad1)
- D236 pad 3: GND -> Net-(D235-Pad6)
- D236 pad 4: VCC -> GND
- D236 pad 5: Net-(D236-Pad5) -> VCC
- D237 pad 1: Net-(D236-Pad6) -> Net-(D237-Pad1)
- D237 pad 2: Net-(D236-Pad5) -> Net-(D236-Pad1)
- D237 pad 3: GND -> Net-(D236-Pad6)
- D237 pad 4: VCC -> GND
- D237 pad 5: Net-(D237-Pad5) -> VCC
- D238 pad 1: Net-(D237-Pad6) -> Net-(D238-Pad1)
- D238 pad 2: Net-(D237-Pad5) -> Net-(D237-Pad1)
- D238 pad 3: GND -> Net-(D237-Pad6)
- D238 pad 4: VCC -> GND
- D238 pad 5: Net-(D238-Pad5) -> VCC
- D239 pad 1: Net-(D238-Pad6) -> Net-(D239-Pad1)
- D239 pad 2: Net-(D238-Pad5) -> Net-(D238-Pad1)
- D239 pad 3: GND -> Net-(D238-Pad6)
- D239 pad 4: VCC -> GND
- D239 pad 5: Net-(D239-Pad5) -> VCC
- D24 pad 1: Net-(D23-Pad6) -> Net-(D24-Pad1)
- D24 pad 2: Net-(D23-Pad5) -> Net-(D23-Pad1)
- D24 pad 3: GND -> Net-(D23-Pad6)
- D24 pad 4: VCC -> GND
- D24 pad 5: Net-(D24-Pad5) -> VCC
- D240 pad 1: Net-(D239-Pad6) -> Net-(D240-Pad1)
- D240 pad 2: Net-(D239-Pad5) -> Net-(D239-Pad1)
- D240 pad 3: GND -> Net-(D239-Pad6)
- D240 pad 4: VCC -> GND
- D240 pad 5: Net-(D240-Pad5) -> VCC
- D241 pad 1: Net-(D240-Pad6) -> Net-(D241-Pad1)
- D241 pad 2: Net-(D240-Pad5) -> Net-(D240-Pad1)
- D241 pad 3: GND -> Net-(D240-Pad6)
- D241 pad 4: VCC -> GND
- D241 pad 5: Net-(D241-Pad5) -> VCC
- D242 pad 1: Net-(D241-Pad6) -> Net-(D242-Pad1)
- D242 pad 2: Net-(D241-Pad5) -> Net-(D241-Pad1)
- D242 pad 3: GND -> Net-(D241-Pad6)
- D242 pad 4: VCC -> GND
- D242 pad 5: Net-(D242-Pad5) -> VCC
- D25 pad 1: Net-(D24-Pad6) -> Net-(D25-Pad1)
- D25 pad 2: Net-(D24-Pad5) -> Net-(D24-Pad1)
- D25 pad 3: GND -> Net-(D24-Pad6)
- D25 pad 4: VCC -> GND
- D25 pad 5: Net-(D25-Pad5) -> VCC
- D26 pad 1: Net-(D25-Pad6) -> Net-(D26-Pad1)
- D26 pad 2: Net-(D25-Pad5) -> Net-(D25-Pad1)
- D26 pad 3: GND -> Net-(D25-Pad6)
- D26 pad 4: VCC -> GND
- D26 pad 5: Net-(D26-Pad5) -> VCC
- D27 pad 1: Net-(D26-Pad6) -> Net-(D27-Pad1)
- D27 pad 2: Net-(D26-Pad5) -> Net-(D26-Pad1)
- D27 pad 3: GND -> Net-(D26-Pad6)
- D27 pad 4: VCC -> GND
- D27 pad 5: Net-(D27-Pad5) -> VCC
- D28 pad 1: Net-(D27-Pad6) -> Net-(D28-Pad1)
- D28 pad 2: Net-(D27-Pad5) -> Net-(D27-Pad1)
- D28 pad 3: GND -> Net-(D27-Pad6)
- D28 pad 4: VCC -> GND
- D28 pad 5: Net-(D28-Pad5) -> VCC
- D29 pad 1: Net-(D28-Pad6) -> Net-(D29-Pad1)
- D29 pad 2: Net-(D28-Pad5) -> Net-(D28-Pad1)
- D29 pad 3: GND -> Net-(D28-Pad6)
- D29 pad 4: VCC -> GND
- D29 pad 5: Net-(D29-Pad5) -> VCC
- D3 pad 1: Net-(D2-Pad6) -> Net-(D3-Pad1)
- D3 pad 2: Net-(D2-Pad5) -> Net-(D2-Pad1)
- D3 pad 3: GND -> Net-(D2-Pad6)
- D3 pad 4: VCC -> GND
- D3 pad 5: Net-(D3-Pad5) -> VCC
- D30 pad 1: Net-(D29-Pad6) -> Net-(D30-Pad1)
- D30 pad 2: Net-(D29-Pad5) -> Net-(D29-Pad1)
- D30 pad 3: GND -> Net-(D29-Pad6)
- D30 pad 4: VCC -> GND
- D30 pad 5: Net-(D30-Pad5) -> VCC
- D31 pad 1: Net-(D30-Pad6) -> Net-(D31-Pad1)
- D31 pad 2: Net-(D30-Pad5) -> Net-(D30-Pad1)
- D31 pad 3: GND -> Net-(D30-Pad6)
- D31 pad 4: VCC -> GND
- D31 pad 5: Net-(D31-Pad5) -> VCC
- D32 pad 1: Net-(D31-Pad6) -> Net-(D32-Pad1)
- D32 pad 2: Net-(D31-Pad5) -> Net-(D31-Pad1)
- D32 pad 3: GND -> Net-(D31-Pad6)
- D32 pad 4: VCC -> GND
- D32 pad 5: Net-(D32-Pad5) -> VCC
- D33 pad 1: Net-(D32-Pad6) -> Net-(D33-Pad1)
- D33 pad 2: Net-(D32-Pad5) -> Net-(D32-Pad1)
- D33 pad 3: GND -> Net-(D32-Pad6)
- D33 pad 4: VCC -> GND
- D33 pad 5: Net-(D33-Pad5) -> VCC
- D34 pad 1: Net-(D33-Pad6) -> Net-(D34-Pad1)
- D34 pad 2: Net-(D33-Pad5) -> Net-(D33-Pad1)
- D34 pad 3: GND -> Net-(D33-Pad6)
- D34 pad 4: VCC -> GND
- D34 pad 5: Net-(D34-Pad5) -> VCC
- D35 pad 1: Net-(D34-Pad6) -> Net-(D35-Pad1)
- D35 pad 2: Net-(D34-Pad5) -> Net-(D34-Pad1)
- D35 pad 3: GND -> Net-(D34-Pad6)
- D35 pad 4: VCC -> GND
- D35 pad 5: Net-(D35-Pad5) -> VCC
- D36 pad 1: Net-(D35-Pad6) -> Net-(D36-Pad1)
- D36 pad 2: Net-(D35-Pad5) -> Net-(D35-Pad1)
- D36 pad 3: GND -> Net-(D35-Pad6)
- D36 pad 4: VCC -> GND
- D36 pad 5: Net-(D36-Pad5) -> VCC
- D37 pad 1: Net-(D36-Pad6) -> Net-(D37-Pad1)
- D37 pad 2: Net-(D36-Pad5) -> Net-(D36-Pad1)
- D37 pad 3: GND -> Net-(D36-Pad6)
- D37 pad 4: VCC -> GND
- D37 pad 5: Net-(D37-Pad5) -> VCC
- D38 pad 1: Net-(D37-Pad6) -> Net-(D38-Pad1)
- D38 pad 2: Net-(D37-Pad5) -> Net-(D37-Pad1)
- D38 pad 3: GND -> Net-(D37-Pad6)
- D38 pad 4: VCC -> GND
- D38 pad 5: Net-(D38-Pad5) -> VCC
- D39 pad 1: Net-(D38-Pad6) -> Net-(D39-Pad1)
- D39 pad 2: Net-(D38-Pad5) -> Net-(D38-Pad1)
- D39 pad 3: GND -> Net-(D38-Pad6)
- D39 pad 4: VCC -> GND
- D39 pad 5: Net-(D39-Pad5) -> VCC
- D4 pad 1: Net-(D3-Pad6) -> Net-(D4-Pad1)
- D4 pad 2: Net-(D3-Pad5) -> Net-(D3-Pad1)
- D4 pad 3: GND -> Net-(D3-Pad6)
- D4 pad 4: VCC -> GND
- D4 pad 5: Net-(D4-Pad5) -> VCC
- D40 pad 1: Net-(D39-Pad6) -> Net-(D40-Pad1)
- D40 pad 2: Net-(D39-Pad5) -> Net-(D39-Pad1)
- D40 pad 3: GND -> Net-(D39-Pad6)
- D40 pad 4: VCC -> GND
- D40 pad 5: Net-(D40-Pad5) -> VCC
- D41 pad 1: Net-(D40-Pad6) -> Net-(D41-Pad1)
- D41 pad 2: Net-(D40-Pad5) -> Net-(D40-Pad1)
- D41 pad 3: GND -> Net-(D40-Pad6)
- D41 pad 4: VCC -> GND
- D41 pad 5: Net-(D41-Pad5) -> VCC
- D42 pad 1: Net-(D41-Pad6) -> Net-(D42-Pad1)
- D42 pad 2: Net-(D41-Pad5) -> Net-(D41-Pad1)
- D42 pad 3: GND -> Net-(D41-Pad6)
- D42 pad 4: VCC -> GND
- D42 pad 5: Net-(D42-Pad5) -> VCC
- D43 pad 1: Net-(D42-Pad6) -> Net-(D43-Pad1)
- D43 pad 2: Net-(D42-Pad5) -> Net-(D42-Pad1)
- D43 pad 3: GND -> Net-(D42-Pad6)
- D43 pad 4: VCC -> GND
- D43 pad 5: Net-(D43-Pad5) -> VCC
- D44 pad 1: Net-(D43-Pad6) -> Net-(D44-Pad1)
- D44 pad 2: Net-(D43-Pad5) -> Net-(D43-Pad1)
- D44 pad 3: GND -> Net-(D43-Pad6)
- D44 pad 4: VCC -> GND
- D44 pad 5: Net-(D44-Pad5) -> VCC
- D45 pad 1: Net-(D44-Pad6) -> Net-(D45-Pad1)
- D45 pad 2: Net-(D44-Pad5) -> Net-(D44-Pad1)
- D45 pad 3: GND -> Net-(D44-Pad6)
- D45 pad 4: VCC -> GND
- D45 pad 5: Net-(D45-Pad5) -> VCC
- D46 pad 1: Net-(D45-Pad6) -> Net-(D46-Pad1)
- D46 pad 2: Net-(D45-Pad5) -> Net-(D45-Pad1)
- D46 pad 3: GND -> Net-(D45-Pad6)
- D46 pad 4: VCC -> GND
- D46 pad 5: Net-(D46-Pad5) -> VCC
- D47 pad 1: Net-(D46-Pad6) -> Net-(D47-Pad1)
- D47 pad 2: Net-(D46-Pad5) -> Net-(D46-Pad1)
- D47 pad 3: GND -> Net-(D46-Pad6)
- D47 pad 4: VCC -> GND
- D47 pad 5: Net-(D47-Pad5) -> VCC
- D48 pad 1: Net-(D47-Pad6) -> Net-(D48-Pad1)
- D48 pad 2: Net-(D47-Pad5) -> Net-(D47-Pad1)
- D48 pad 3: GND -> Net-(D47-Pad6)
- D48 pad 4: VCC -> GND
- D48 pad 5: Net-(D48-Pad5) -> VCC
- D49 pad 1: Net-(D48-Pad6) -> Net-(D49-Pad1)
- D49 pad 2: Net-(D48-Pad5) -> Net-(D48-Pad1)
- D49 pad 3: GND -> Net-(D48-Pad6)
- D49 pad 4: VCC -> GND
- D49 pad 5: Net-(D49-Pad5) -> VCC
- D5 pad 1: Net-(D4-Pad6) -> Net-(D5-Pad1)
- D5 pad 2: Net-(D4-Pad5) -> Net-(D4-Pad1)
- D5 pad 3: GND -> Net-(D4-Pad6)
- D5 pad 4: VCC -> GND
- D5 pad 5: Net-(D5-Pad5) -> VCC
- D50 pad 1: Net-(D49-Pad6) -> Net-(D50-Pad1)
- D50 pad 2: Net-(D49-Pad5) -> Net-(D49-Pad1)
- D50 pad 3: GND -> Net-(D49-Pad6)
- D50 pad 4: VCC -> GND
- D50 pad 5: Net-(D50-Pad5) -> VCC
- D51 pad 1: Net-(D50-Pad6) -> Net-(D51-Pad1)
- D51 pad 2: Net-(D50-Pad5) -> Net-(D50-Pad1)
- D51 pad 3: GND -> Net-(D50-Pad6)
- D51 pad 4: VCC -> GND
- D51 pad 5: Net-(D51-Pad5) -> VCC
- D52 pad 1: Net-(D51-Pad6) -> Net-(D52-Pad1)
- D52 pad 2: Net-(D51-Pad5) -> Net-(D51-Pad1)
- D52 pad 3: GND -> Net-(D51-Pad6)
- D52 pad 4: VCC -> GND
- D52 pad 5: Net-(D52-Pad5) -> VCC
- D53 pad 1: Net-(D52-Pad6) -> Net-(D53-Pad1)
- D53 pad 2: Net-(D52-Pad5) -> Net-(D52-Pad1)
- D53 pad 3: GND -> Net-(D52-Pad6)
- D53 pad 4: VCC -> GND
- D53 pad 5: Net-(D53-Pad5) -> VCC
- D54 pad 1: Net-(D53-Pad6) -> Net-(D54-Pad1)
- D54 pad 2: Net-(D53-Pad5) -> Net-(D53-Pad1)
- D54 pad 3: GND -> Net-(D53-Pad6)
- D54 pad 4: VCC -> GND
- D54 pad 5: Net-(D54-Pad5) -> VCC
- D55 pad 1: Net-(D54-Pad6) -> Net-(D55-Pad1)
- D55 pad 2: Net-(D54-Pad5) -> Net-(D54-Pad1)
- D55 pad 3: GND -> Net-(D54-Pad6)
- D55 pad 4: VCC -> GND
- D55 pad 5: Net-(D55-Pad5) -> VCC
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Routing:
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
